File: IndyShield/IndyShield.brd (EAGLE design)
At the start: 69.9 x 78.1 mm, 18 parts, among them U1 ARDUINOR3-BPLACE

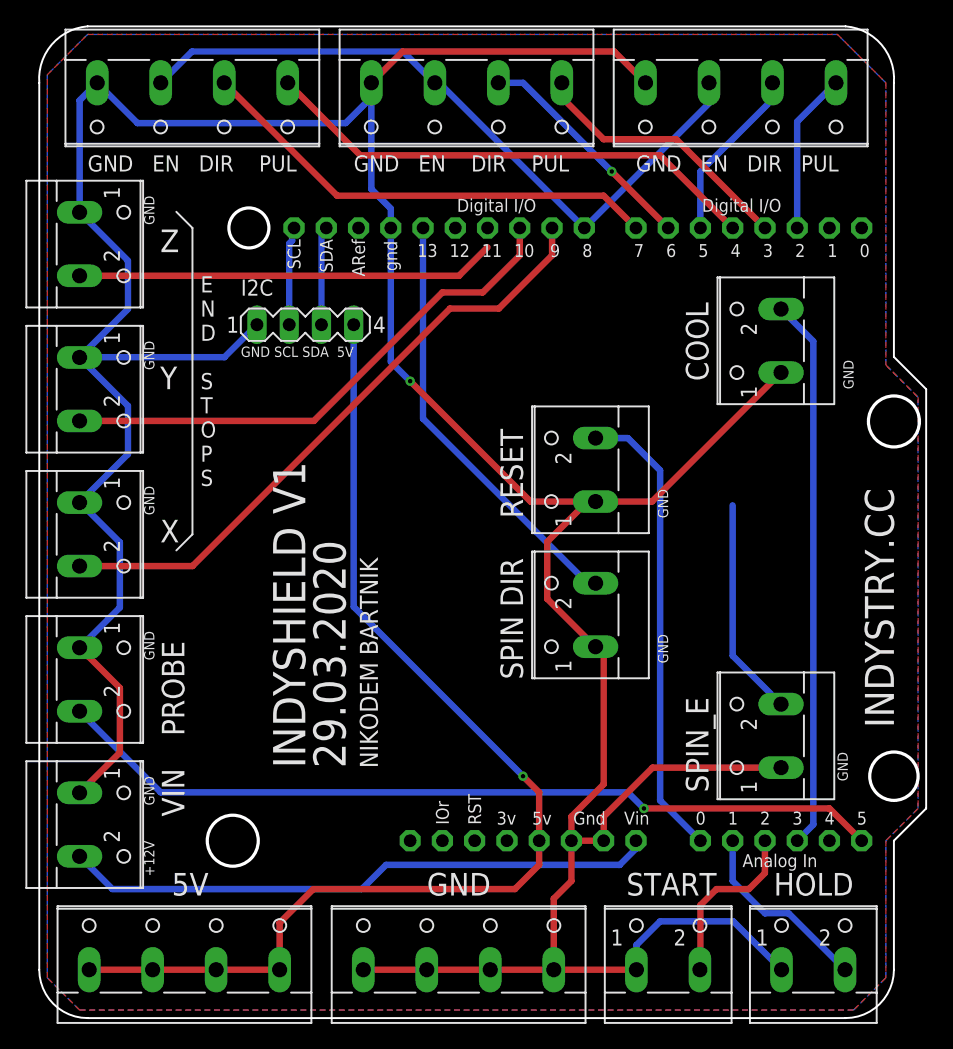
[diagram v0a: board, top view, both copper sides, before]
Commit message: Updated IndyShield to V2
Swapped Z axis limit with spindle enable as it should be for current version of GRBL
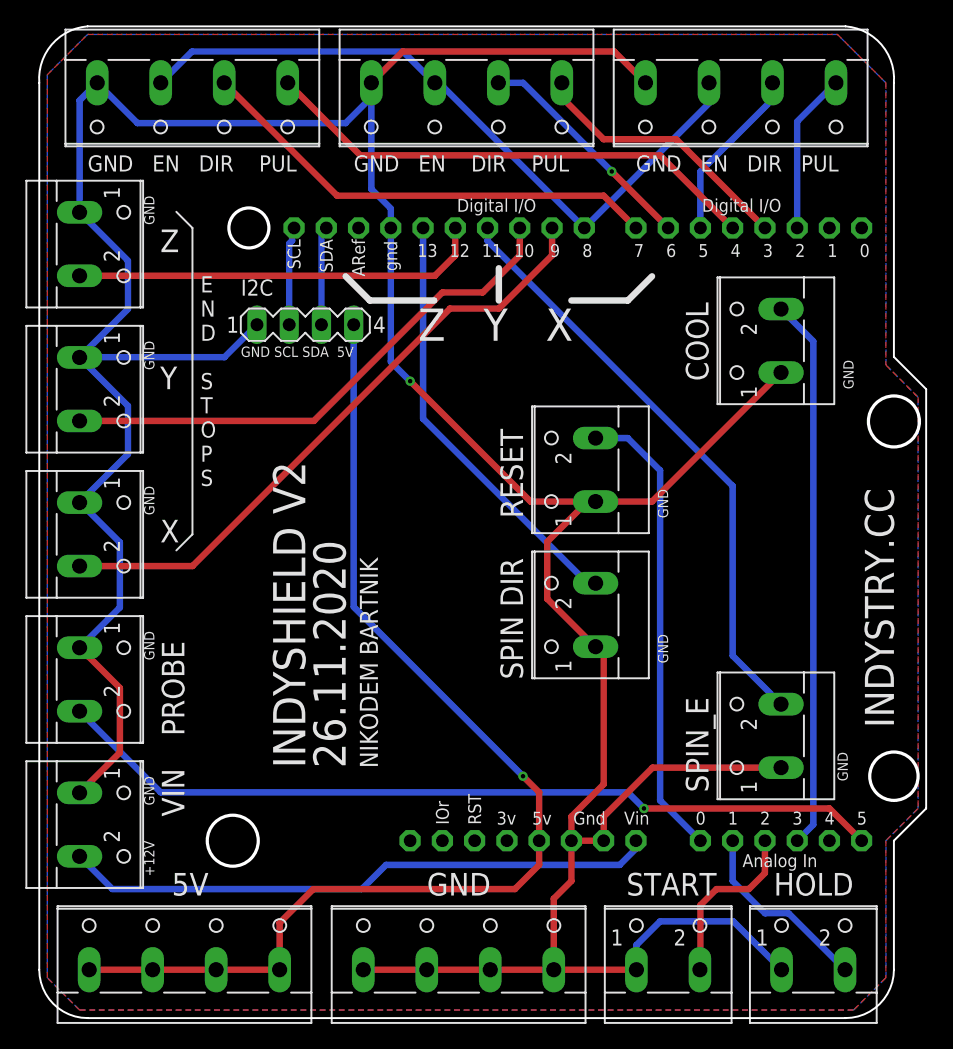
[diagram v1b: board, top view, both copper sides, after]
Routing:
- net SPIN_E: track 17.2 -> 47.1 mm
- net LIM_Z: track 33.1 -> 32.4 mm
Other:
- board text added: "26.11.2020"
- board text added: "INDYSHIELD V2"
- board text added: "Z Y X"
- board text removed: "29.03.2020"
- board text removed: "INDYSHIELD V1"
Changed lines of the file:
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@@
 </layers>
 <board>
-<fusionsync huburn="a.cGVyc29uYWw6dWUyOTVlY2M3" projecturn="a.cGVyc29uYWw6dWUyOTQ1MGNhIzIwMTUxMDAxMTc3NTg0ODE" f3durn="urn:adsk.wipprod:dm.lineage:imIz-XI3STe14i4ZA2mIJQ" pcbguid="5a41f7d2-153f-4675-94ec-d0aa77b1afd1" lastpulledtime="" lastsyncedchangeguid="178d8192-3e9e-a262-734b-2777a9755d98"/>
+<fusionsync huburn="a.cGVyc29uYWw6dWUyOTVlY2M3" projecturn="a.cGVyc29uYWw6dWUyOTQ1MGNhIzIwMTUxMDAxMTc3NTg0ODE" f3durn="urn:adsk.wipprod:dm.lineage:imIz-XI3STe14i4ZA2mIJQ" pcbguid="5a41f7d2-153f-4675-94ec-d0aa77b1afd1" lastpulledtime="" lastsyncedchangeguid="24f6117a-ca31-6ca8-8376-37b6e06dccf4"/>
 <plain>
 <wire x1="35.56" y1="15.24" x2="35.56" y2="85.09" width="0.1524" layer="20"/>
@@
 <text x="88.9" y="22.86" size="1.778" layer="25" rot="R180">START</text>
 <text x="99.695" y="22.86" size="1.778" layer="25" rot="R180">HOLD</text>
-<text x="56.515" y="31.115" size="2.54" layer="25" rot="R90">INDYSHIELD V1</text>
-<text x="59.69" y="31.115" size="2.54" layer="25" rot="R90">29.03.2020</text>
+<text x="56.515" y="31.115" size="2.54" layer="25" rot="R90">INDYSHIELD V2</text>
+<text x="59.69" y="31.115" size="2.54" layer="25" rot="R90">26.11.2020</text>
 <text x="62.23" y="31.115" size="1.4224" layer="25" rot="R90">NIKODEM BARTNIK</text>
 <text x="85.09" y="50.8" size="0.8128" layer="25" rot="R90">GND</text>
@@
 <text x="43.815" y="30.48" size="0.8128" layer="25" rot="R270">GND</text>
 <text x="43.815" y="25.4" size="0.8128" layer="25" rot="R270">+12V</text>
+<text x="65.405" y="64.77" size="2.54" layer="25">Z   Y   X</text>
+<wire x1="77.47" y1="67.945" x2="81.915" y2="67.945" width="0.508" layer="25"/>
+<wire x1="81.915" y1="67.945" x2="83.82" y2="69.85" width="0.508" layer="25"/>
+<wire x1="71.755" y1="67.945" x2="71.755" y2="70.485" width="0.508" layer="25"/>
+<wire x1="66.675" y1="67.945" x2="61.595" y2="67.945" width="0.508" layer="25"/>
+<wire x1="61.595" y1="67.945" x2="59.69" y2="69.85" width="0.508" layer="25"/>
 </plain>
 <attributes>
@@
 <signal name="LIM_Z">
 <contactref element="LZ" pad="2"/>
-<wire x1="38.735" y1="69.89" x2="68.62" y2="69.89" width="0.508" layer="1"/>
-<wire x1="68.62" y1="69.89" x2="70.866" y2="72.136" width="0.508" layer="1"/>
+<wire x1="38.735" y1="69.89" x2="66.715" y2="69.89" width="0.508" layer="1"/>
+<wire x1="66.715" y1="69.89" x2="68.2625" y2="71.4375" width="0.508" layer="1"/>
 <contactref element="U1" pad="D12"/>
-<wire x1="70.866" y1="72.136" x2="68.326" y2="73.66" width="0" layer="19" extent="1-1"/>
+<wire x1="68.2625" y1="71.4375" x2="68.326" y2="71.501" width="0.508" layer="1"/>
+<wire x1="68.326" y1="71.501" x2="68.326" y2="73.66" width="0.508" layer="1"/>
 </signal>
 <signal name="SPIN_E">
 <contactref element="SPIN_E" pad="2"/>
 <wire x1="93.98" y1="36.155" x2="90.17" y2="39.965" width="0.508" layer="16"/>
-<wire x1="90.17" y1="39.965" x2="90.17" y2="51.816" width="0.508" layer="16"/>
 <contactref element="U1" pad="D11"/>
-<wire x1="90.17" y1="51.816" x2="70.866" y2="73.66" width="0" layer="19" extent="16-16"/>
+<wire x1="70.866" y1="72.644" x2="70.866" y2="73.66" width="0.508" layer="16"/>
+<wire x1="90.17" y1="39.965" x2="90.17" y2="53.34" width="0.508" layer="16"/>
+<wire x1="90.17" y1="53.34" x2="70.866" y2="72.644" width="0.508" layer="16"/>
 </signal>
 <signal name="SPIN_DIR">
